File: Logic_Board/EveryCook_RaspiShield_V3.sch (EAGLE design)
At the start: 95 parts, among them IC1 TLP281-4, IC2 TLP281-4, J1 6P-2.54mm, J4 6P-2.54mm, J5 JUMPERSMD, Q2 IRLZ44N, U1 AD7794BRUZ, U2 PCA9685PW, U4 78M05, U7 CJ1117-3.3

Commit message: Schematic of logic board finished, only audio amp missing. Board ripped up for redraw
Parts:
- removed C4: 100uF/16V, Discrete:CAP-ELECTRO-C
- removed C8: 0.1uF, Discrete:C-0603
- removed D3: M7, Discrete:D-SMA
- removed IC1: TLP281-4, IC:TLP521-4
- removed J1: 6P-2.54mm, Connector:HEADER-6P-80/40MIL
- removed J14: (no value), Connector:HEADER-2P-5.0
- removed J4: 6P-2.54mm, Connector:HEADER-6P-65/35MIL
- removed J5: JUMPERSMD, Discrete:JUMPERSMD
- removed L2: 47uH, Discrete:L0630
- removed R1, R10, R11, R12, R13, R18, R19, R20, R21, R26, R27, R28, R29, R6, R7, R8, R9: 1k, Discrete:R-0603
- removed R14: 51k, Discrete:R-0603
- removed R15, R22, R23, R24, R25: 10k, Discrete:R-0603
- removed R16: 2k, Discrete:R-0603
- removed R5: 4.7k, Discrete:R-0603
- removed U$2: LM2596, IC:LM2596
- removed U13, U14, U15, U16, U17: (no value), Connector:RJ45-N
- removed U2: PCA9685PW, wia:PCA9685PW
- added BUT1, BUT2, BUT3, C_CLOSE, C_LOCK, FAN, I2C, P_LOCK, THSTAT_POT: (no value), pinhead:PINHD-1X2
- added C14: 22pF, Discrete:C-0603
- added C15: 0.1uF, Discrete:C-0603
- added DISPLAY, POWR_BRD: (no value), pinhead:PINHD-2X6
- added Q1: 8 MHz, crystal:CRYSTALHC49UP
- added Q3: BSP372, infineon:BSP613P
- added R3, R40, R45, R46: 10k, Discrete:R-0603
- added R39, R4, R44, R47, R48: 1k, Discrete:R-0603
- added T2: (no value), zetex:NPN_PNPSM8
- added VALVE+PROXSW: (no value), pinhead:PINHD-1X4
- added X1, X2, X3, X4, X5: MINI-USB_4P-85-32006-601-1, con-cypressindustries:MINI-USB_4P-85-32006-601-1
- C3: value 220uF/35V -> 22pF; device Discrete:CAP-ELECTRO-G -> Discrete:C-0603
- IC2: value TLP281-4 -> ATMEGA644A; device IC:TLP521-4 -> atmel:ATMEGA644A
- Q2: value IRLZ44N -> BSP372; device Discrete:MOSFET-N-D2PAK -> infineon:BSP613P; IMAX (none) -> 1.7A; MF (none) -> Infineon; VMAX (none) -> 100V
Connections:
- removed net +24V: C2.+, C3.+, J2.2, U$2.VIN, U4.IN
- removed net 3V3: C10.2, C17.2, C18.2, C6.+, C9.2, IC1.10, IC1.12, IC1.14, IC1.16, R26.2, R27.2, R28.2, R29.2, U1.DVDD, U16.2, U16.6, U16.8, U17.10, U17.9, U2.VDD, U7.OUT, U7.TAB
- removed net BUTTON: IC2.11, IC2.13, IC2.15, IC2.9, J4.2
- removed net CS: U$1.24-SPI-CE0-N, U1.~CS
- removed net D5V: C1.+, C4.+, C8.2, J5.2, L2.2, U$2.FB, U15.6, U7.IN
- removed net GPIO1: R41.2, U$1.11-GPIO0, U16.1
- removed net GPIO2: R42.2, U$1.13-GPIO2, U16.3
- removed net KEY1: IC2.16, R5.1
- removed net KEY1S: IC2.2, U$1.12-GPIO1
- removed net KEY2: IC2.14, R14.1
- removed net KEY2S: IC2.4, U$1.16-GPIO4
- removed net KEY3: IC2.12, R15.1
- removed net KEY3S: IC2.6, U$1.18-GPIO5
- removed net KEY4: IC2.10, R16.1
- removed net KEY4S: IC2.8, U$1.22-GPIO6
- removed net LED: IC1.2, J4.3
- removed net LED-1: R6.2, U17.1
- removed net LED-2: R7.2, U17.2
- removed net LED-3: R8.2, U17.3
- removed net LED-4: R9.2, U17.4
- removed net LED-5: R10.2, U17.5
- removed net LED-6: R11.2, U17.6
- removed net LED-7: R12.2, U17.7
- removed net LED-8: R13.1, U17.8
- removed net LED1: IC1.4, J4.4
- removed net LED1S: IC1.13, R23.2, U$1.8-TX
- removed net LED2: IC1.6, J4.5
- removed net LED2S: IC1.11, R24.2, U$1.10-RX
- removed net LED3: IC1.8, J4.6
- removed net LED3S: IC1.9, R25.2, U$1.26-SPI-CE1-N
- removed net LEDS: IC1.15, R22.2, U$1.7-GPIO7
- removed net MVCC: J14.1, J3.1
- removed net N$13: R1.2, U2.LED0
- removed net N$14: J1.2, U2.LED11
- removed net N$20: IC1.1, R18.1
- removed net N$21: IC1.3, R19.1
- removed net N$22: IC1.5, R20.1
- removed net N$23: IC1.7, R21.1
- removed net N$25: R6.1, U2.LED2
- removed net N$26: R7.1, U2.LED3
- removed net N$27: R8.1, U2.LED4
- removed net N$28: R9.1, U2.LED5
- removed net N$29: R10.1, U2.LED6
- removed net N$3: Q2.G, R1.1
- removed net N$30: R11.1, U2.LED7
- removed net N$31: R12.1, U2.LED8
- removed net N$32: R13.2, U2.LED9
- removed net N$33: J1.3, U2.LED12
- removed net N$34: J1.4, U2.LED13
- removed net N$35: J1.5, U2.LED14
- removed net N$36: J1.6, U2.LED15
- removed net N$4: J1.1, U2.LED10
- removed net N$67: IC2.1, R26.1
- removed net N$68: IC2.3, R27.1
- removed net N$69: IC2.5, R28.1
- removed net N$70: IC2.7, R29.1
- removed net N$91: U15.7
- removed net SCL: U$1.5-SCL0, U2.SCL
- removed net SDA: U$1.3-SDA0, U2.SDA
- removed net SERVO_SIG: U15.8, U2.LED1
- removed net VCC: J4.1, R14.2, R15.2, R16.2, R18.2, R19.2, R20.2, R21.2, R5.2
- new net +12V: C2.+, FAN.1, J3.1, U4.IN, VALVE+PROXSW.1
- new net +3V3: C10.2, C15.2, C17.2, C18.2, C6.+, C9.2, IC2.VCC, IC2.VCC@2, POWR_BRD.4, R3.2, R45.1, U1.DVDD, U7.OUT
- new net +5V: C1.+, J2.2, R46.2, T2A.E, U7.IN
- new net DAEMON_RST_LINE: IC2.(PCINT16/SCL)PC0, R44.1
- new net FAN_PWM: Q2.G, R4.1
- new net IH_OFF: IC2.(PCINT26/INT0)PD2, POWR_BRD.9
- new net IH_ON: POWR_BRD.5
- new net IH_PWR: IC2.(PCINT30/OC2B/ICP)PD6, POWR_BRD.1
- new net IH_RUN: IC2.(PCINT27/INT1)PD3, POWR_BRD.7
- new net IH_THERMISTOR: IC2.(PCINT1/ADC1)PA1, POWR_BRD.2, R40.2
- new net MOT_PWM: IC2.(PCINT29/OC1A)PD5, POWR_BRD.3
- new net N$10: IC2.(PCINT31/OC2A)PD7, R4.2
- new net N$11: DISPLAY.12, IC2.(PCINT18/TCK)PC2
- new net N$12: I2C.2, U$1.3-SDA0
- new net N$15: DISPLAY.11, IC2.(PCINT19/TMS)PC3
- new net N$16: DISPLAY.10, IC2.(PCINT20/TDO)PC4
- new net N$17: DISPLAY.9, IC2.(PCINT21/TDI)PC5
- new net N$18: DISPLAY.8, IC2.(PCINT22/TOSC1)PC6
- new net N$19: DISPLAY.7, IC2.(PCINT23/TOSC2)PC7
- new net N$37: DISPLAY.6, IC2.(PCINT8/XCK0/T0)PB0
- new net N$38: DISPLAY.5, IC2.(PCINT9/CLKO/T1)PB1
- new net N$39: DISPLAY.4, IC2.(PCINT10/INT2/AIN0)PB2
- new net N$41: DISPLAY.3, IC2.(PCINT11/OC0A/AIN1)PB3
- new net N$43: DISPLAY.1, IC2.(PCINT12/OC0B/!SS!)PB4
- new net N$49: DISPLAY.2, IC2.(PCINT0/ADC0)PA0
- new net N$50: I2C.1, U$1.5-SCL0
- new net N$51: FAN.2, Q2.D@1
- new net N$52: IC2.(PCINT24/RXD0)PD0, U$1.8-TX
- new net N$54: IC2.(PCINT25/TXD0)PD1, U$1.10-RX
- new net N$55: IC2.(PCINT14/MISO)PB6, U$1.16-GPIO4
- new net N$56: IC2.(PCINT13/MOSI)PB5, U$1.12-GPIO1
- new net N$59: C_CLOSE.1, IC2.(PCINT7/ADC7)PA7
- new net N$6: IC2.RESET, R3.1
- new net N$60: C_LOCK.1, IC2.(PCINT6/ADC6)PA6
- new net N$61: IC2.(PCINT5/ADC5)PA5, P_LOCK.1
- new net N$62: BUT2.1
- new net N$63: BUT3.1
- new net N$64: R39.2
- new net N$66: BUT1.1, R39.1, R44.2, R45.2
- new net N$7: C14.1, IC2.XTAL1, Q1.1
- new net N$71: R47.2, T2B.B
- new net N$72: R46.1, T2A.B, T2B.C1
- new net N$77: Q3.D@1, VALVE+PROXSW.2
- new net N$8: IC2.(PCINT15/SCK)PB7, U$1.18-GPIO5
- new net PROX_SWI: IC2.(PCINT2/ADC2)PA2, VALVE+PROXSW.3
- new net RPI_RST: IC2.(PCINT17/SDA)PC1, R47.1
- new net SAFETY_CHAIN: IC2.(PCINT4/ADC4)PA4
- new net VALVE_OPEN: Q3.G, R48.1
- net GND: now also BUT1.2, BUT2.2, BUT3.2, C14.2, C15.1, C3.2, C_CLOSE.2, C_LOCK.2, IC2.GND, IC2.GND@3, P_LOCK.2, Q2.S, Q3.S, R40.1, T2B.E, THSTAT_POT.2, U1.~CS, VALVE+PROXSW.4, X1.4, X2.4, X3.4, X4.4, X5.4; no longer C3.-, C4.-, C8.1, D3.+, R22.1, R23.1, R24.1, R25.1, U$2.GND, U$2.ON/OFF, U13.3, U13.4, U14.3, U14.4, U15.3, U15.4, U16.5, U2.A0, U2.A1, U2.A2, U2.A3, U2.A4, U2.A5, U2.EXTCLK, U2.VSS, U2.~OE, U4.GND
- net GPIO3: no longer U$1.15-GPIO3, U16.7
- net L5V: now also X1.1, X2.1, X3.1, X4.1, X5.1; no longer U13.5, U13.6, U14.5, U14.6, U15.5
- net LOADCELL1_SIG+: now also X2.2; no longer U13.7
- net LOADCELL1_SIG-: now also X2.3; no longer U13.8
- net LOADCELL2_SIG+: now also X1.2; no longer U13.1
- net LOADCELL2_SIG-: now also X1.3; no longer U13.2
- net LOADCELL3_SIG+: now also X4.2; no longer U14.7
- net LOADCELL3_SIG-: now also X4.3; no longer U14.8
- net LOADCELL4_SIG+: now also X3.2; no longer U14.1
- net LOADCELL4_SIG-: now also X3.3; no longer U14.2
- net N$2: now also C3.1, IC2.XTAL2, Q1.2; no longer J14.2, Q2.D
- net N$58: now also T2A.C1; no longer J5.1
- net N$65: now also IC2.(PCINT3/ADC3)PA3, R48.2; no longer D3.-, L2.1, U$2.OUTPUT
- net PGND: no longer Q2.S, U13.10, U13.9, U14.10, U14.9, U15.10, U15.9, U16.10, U16.9
- net PRESS_SIG+: now also X5.2; no longer U15.1
- net PRESS_SIG-: now also X5.3; no longer U15.2
- net TEMPER_SIG+: now also THSTAT_POT.1; no longer U16.4
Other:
- note removed: "7-Seg LED Conn."
- note removed: "Motor Conn."
- note removed: "PT 1000"
- note removed: "Reserve PWM Pads"
- note removed: "black"
- note removed: "blue"
- note removed: "bluew"
- note removed: "brown"
- note removed: "brownw"
- note removed: "button 2"
- note removed: "button 3"
- note removed: "button1"
- note removed: "green"
- note removed: "greenw"
- note removed: "on RJ45 cable"
- note removed: "on loadcells"
- note removed: "red"
- note removed: "redw"
- note removed: "servo brown"
- note removed: "servo orange"
- note removed: "servo red"
- note removed: "sig -"
- note removed: "sig 5V"
- note removed: "sig gnd"
- note removed: "sig+"
- note removed: "white"
- moved on the sheet: C1, C10, C12, C17, C18, C2, C6, C7, J2, J3, U4, U7

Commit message: Logic board all routed...
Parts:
- removed R41, R42, R43: 10k, Discrete:R-0603
- removed THSTAT_POT: (no value), pinhead:PINHD-1X2
- removed U$1: RASPBERRY-PI, RaspberryPi:RASPBERRY-PI
- added AIN_GND, AIN_SIG: (no value), wirepad:2,15/1,0
- added C16, C8: 10uF, Discrete:C-0603
- added C38: 100uF/25V, Discrete:CAP-ELECTRO-B
- added C4: 220pF, Discrete:C-0603
- added IC1: LM386MM-1, linear:LM386MM-1
- added R1, R5: 5k, Discrete:R-0603
- added R6, R7: 10k, Discrete:R-0603
- added RASPI_CONNECTOR_(TOP): (no value), pinhead:PINHD-2X13
- added SP1: AL23P, buzzer:AL23P
- added TEMP: (no value), pinhead:PINHD-1X2
- R3: value 10k -> 22k
- T2: value (none) -> ZDT6790
- renumbered X1 to LC2, X2 to LC1, X3 to LC4, X4 to LC3, X5 to PRESS
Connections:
- removed net GPIO3: R43.2
- removed net N$40: U$1.19-SPI-MOSI, U1.DIN
- new net MOSI: RASPI_CONNECTOR_(TOP).19, U1.DIN
- new net N$14: IC1.+IN, R1.2, R5.1
- new net N$22: C16.1, C38.+, IC1.OUT
- new net N$23: C38.-, SP1.1
- new net N$27: AIN_SIG.P, C4.2
- new net N$3: C4.1, R5.2
- net +3V3: now also IC2.AVCC, IC2.VCC@1, R6.1, R7.1
- net +5V: now also C16.2, IC1.VS
- net GND: now also AIN_GND.P, C8.1, IC1.-IN, IC1.GND, IC2.GND@1, IC2.GND@2, R1.1, RASPI_CONNECTOR_(TOP).6, SP1.2, TEMP.2; no longer R41.1, R42.1, R43.1, THSTAT_POT.2, U$1.6-GND
- net IH_ON: now also IC2.(PCINT28/OC1B)PD4
- net MISO: now also RASPI_CONNECTOR_(TOP).21; no longer U$1.21-SPI-MISO
- net N$12: now also RASPI_CONNECTOR_(TOP).3; no longer U$1.3-SDA0
- net N$50: now also RASPI_CONNECTOR_(TOP).5; no longer U$1.5-SCL0
- net N$52: now also RASPI_CONNECTOR_(TOP).8; no longer U$1.8-TX
- net N$54: now also RASPI_CONNECTOR_(TOP).10; no longer U$1.10-RX
- net N$55: now also RASPI_CONNECTOR_(TOP).16; no longer U$1.16-GPIO4
- net N$56: now also RASPI_CONNECTOR_(TOP).12; no longer U$1.12-GPIO1
- net N$58: now also RASPI_CONNECTOR_(TOP).2; no longer U$1.2-+5V
- net N$6: now also C8.2, RASPI_CONNECTOR_(TOP).11
- net N$62: now also R7.2, RASPI_CONNECTOR_(TOP).24
- net N$63: now also R6.2, RASPI_CONNECTOR_(TOP).26
- net N$64: now also RASPI_CONNECTOR_(TOP).22
- net N$8: now also RASPI_CONNECTOR_(TOP).18; no longer U$1.18-GPIO5
- net SAFETY_CHAIN: now also POWR_BRD.11
- net SCLK: now also RASPI_CONNECTOR_(TOP).23; no longer U$1.23-SPI-SCLK
- net TEMPER_SIG+: now also TEMP.1; no longer THSTAT_POT.1

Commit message: changed all 0606 to 0805 package for R and C.
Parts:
- C10, C11, C12, C14, C15, C16, C17, C18, C19, C20, C21, C22, C23, C24, C25, C26, C27, C28, C29, C3, C30, C31, C32, C33, C34, C35, C36, C37, C4, C5, C9: device Discrete:C-0603 -> rcl:C-EUC0805
- C13: device Discrete:C-0805 -> rcl:C-EUC0805
- C8: value 10uF -> 100nF; device Discrete:C-0603 -> rcl:C-EUC0805
- R1, R17, R3, R30, R31, R32, R33, R34, R35, R36, R37, R38, R39, R4, R40, R44, R45, R46, R47, R48, R5, R6, R7: device Discrete:R-0603 -> rcl:R-EU_R0805
- R2: value 22k -> 2.2k; device Discrete:R-0603 -> rcl:R-EU_R0805
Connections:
- net +3V3: now also U7.TAB
- net GND: now also U4.GND
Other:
- note removed: "KE43------ ON/OFF"
- note removed: "KEY1--------FUNSION"
- note removed: "KEY2------ -"
- note removed: "KEY3------ +"
- note removed: "SIG1--------MIN"
- note removed: "SIG2--------POWER"
- note removed: "SIG3--------MAX"
- note removed: "SIG4--------HOTPOT"
- note removed: "SIG5--------MID"
- note removed: "SIG6--------HEAT"
- moved on the sheet: C1, C2, C6, C7, J2, J3, LC1, LC2, LC3, LC4, PRESS, U4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

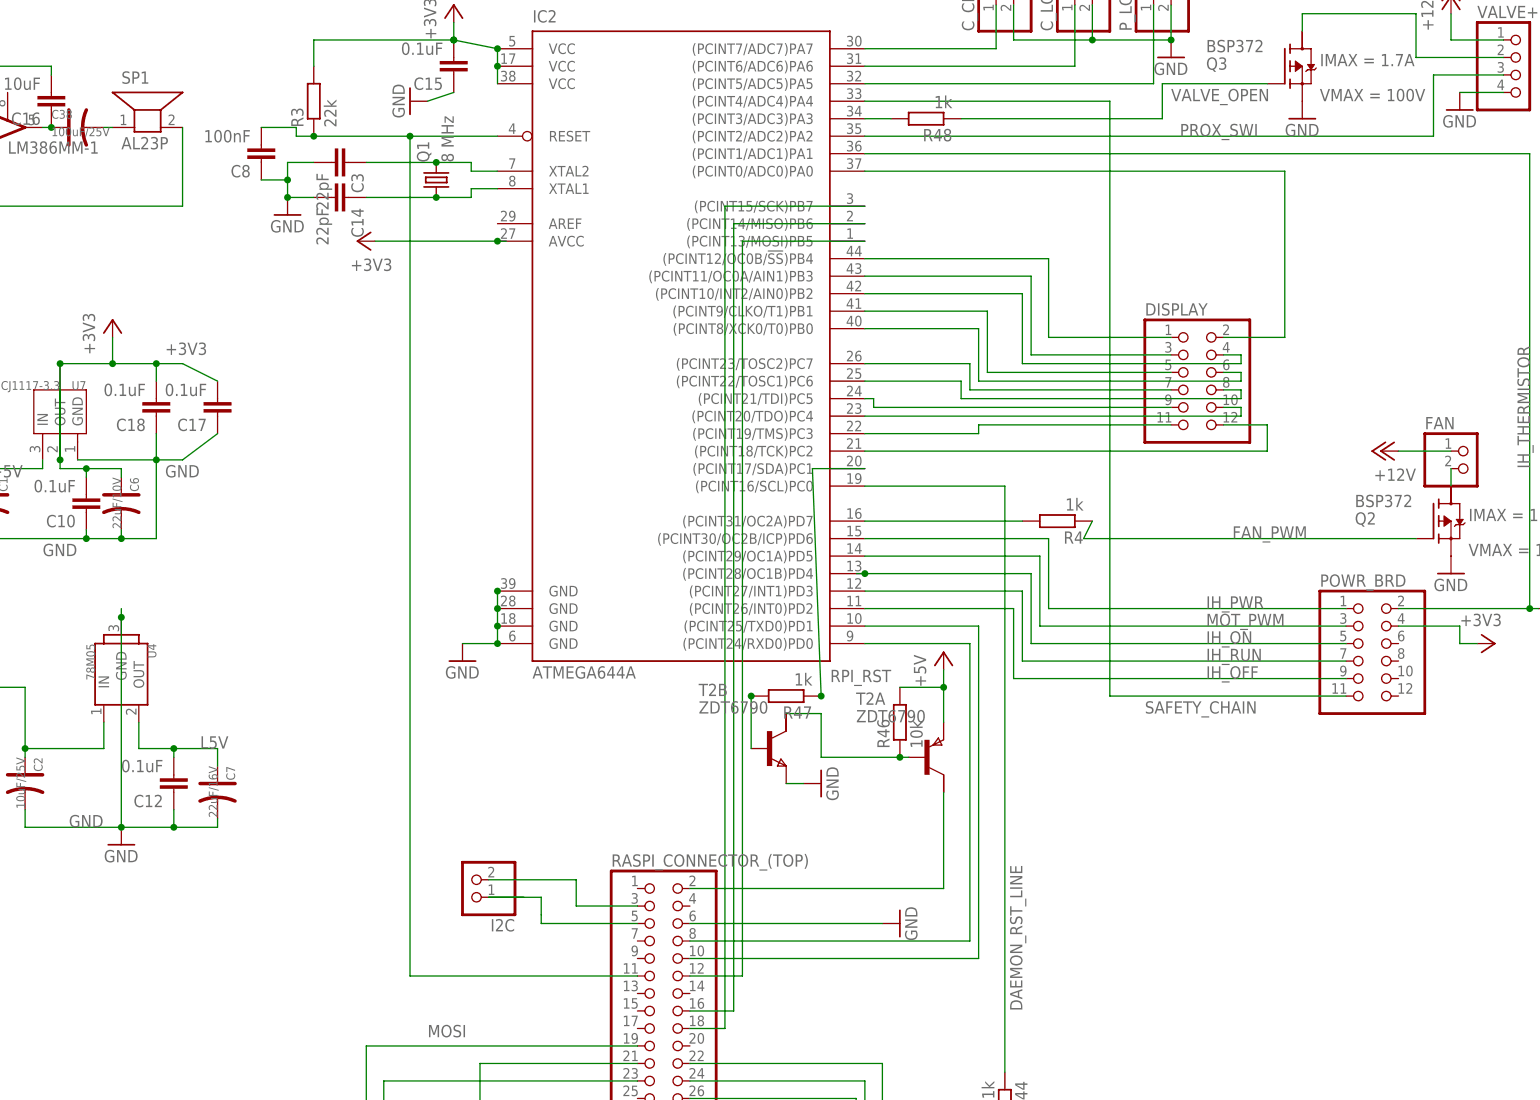
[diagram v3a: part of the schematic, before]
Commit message: Cleaned up the logic board. added safety chain board.
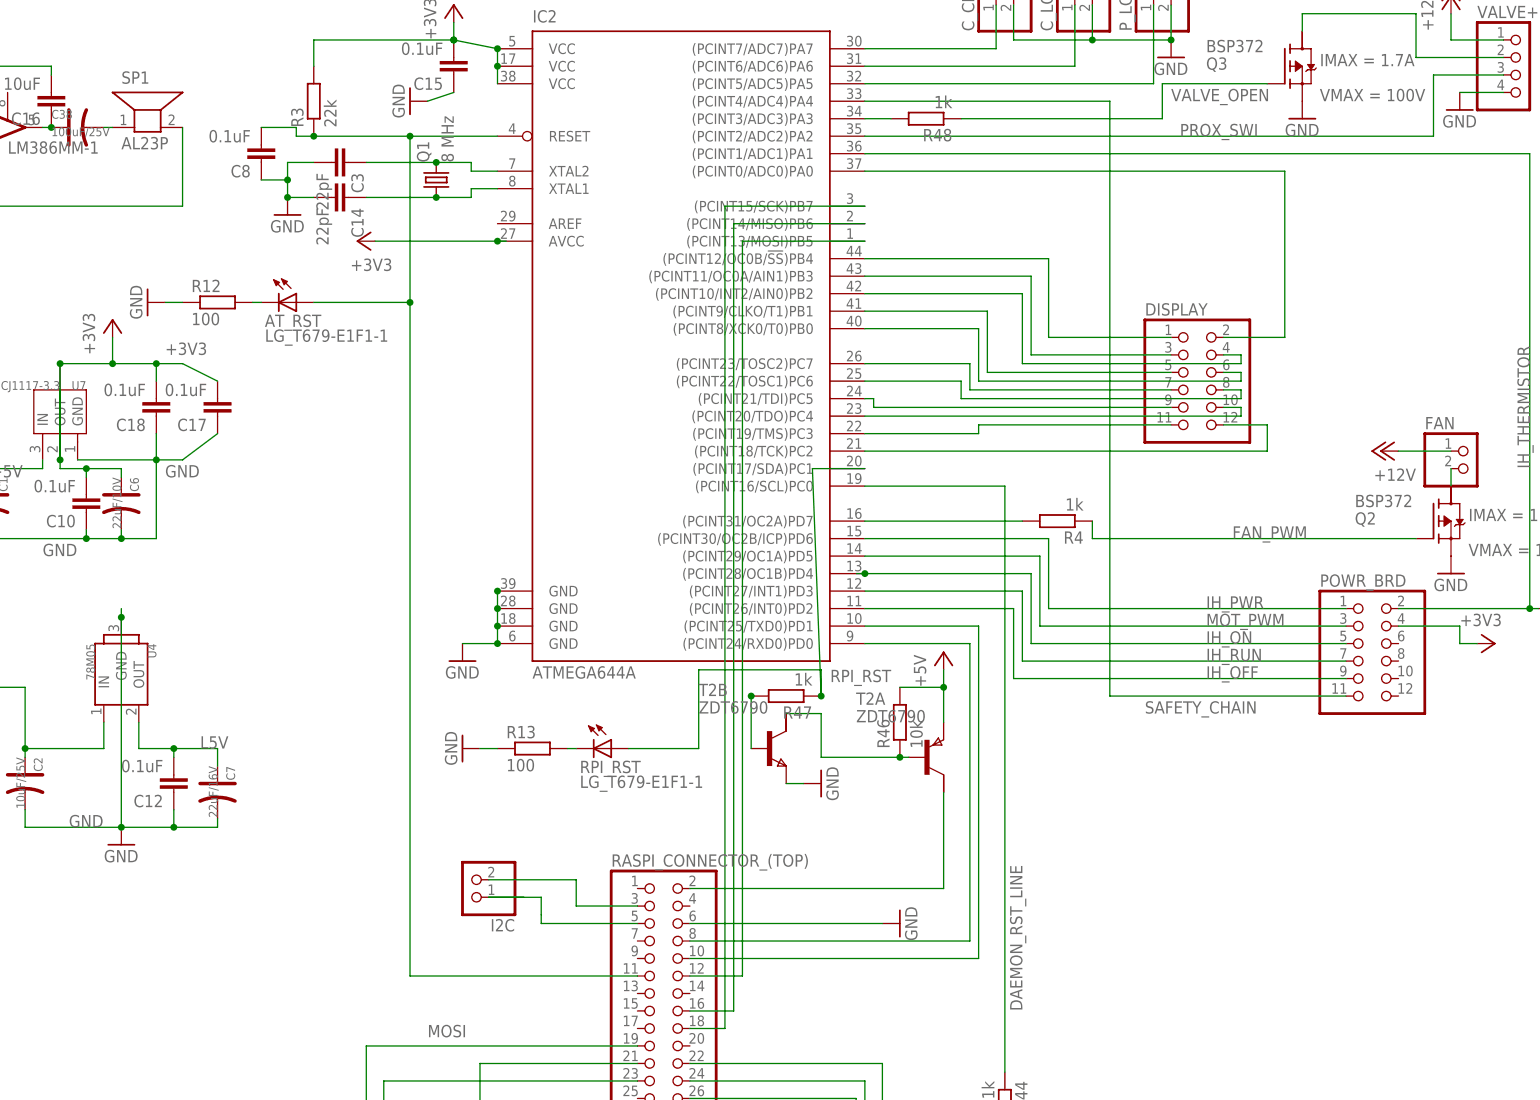
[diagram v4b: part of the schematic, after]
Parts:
- added AT_RST, RPI_RST: LG_T679-E1F1-1, led:LG_T679-E1F1-1
- added R12, R13: 100, rcl:R-EU_R0805
- C8: value 100nF -> 0.1uF
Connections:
- removed net N$6: C8.2, IC2.RESET, R3.1, RASPI_CONNECTOR_(TOP).11
- new net ATMEL_RST: AT_RST.A, C8.2, IC2.RESET, R3.1, RASPI_CONNECTOR_(TOP).11
- new net N$32: AT_RST.C, R12.2
- new net N$34: R13.2, RPI_RST.C
- net GND: now also R12.1, R13.1
- net RPI_RST: now also RPI_RST.A
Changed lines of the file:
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@@
 <setting verticaltext="up"/>
 </settings>
-<grid distance="0.05" unitdist="inch" unit="inch" style="lines" multiple="1" display="yes" altdistance="0.01" altunitdist="inch" altunit="inch"/>
+<grid distance="0.05" unitdist="inch" unit="inch" style="lines" multiple="1" display="no" altdistance="0.025" altunitdist="inch" altunit="inch"/>
 <layers>
 <layer number="1" name="Top" color="4" fill="1" visible="no" active="no"/>
@@
 <part name="R6" library="rcl" deviceset="R-EU_" device="R0805" value="10k"/>
 <part name="R7" library="rcl" deviceset="R-EU_" device="R0805" value="10k"/>
-<part name="C8" library="rcl" deviceset="C-EU" device="C0805" value="100nF"/>
+<part name="C8" library="rcl" deviceset="C-EU" device="C0805" value="0.1uF"/>
 <part name="GND25" library="supply1" deviceset="GND" device=""/>
+<part name="AT_RST" library="led" deviceset="*_T679-?-1" device="E1F1" technology="LG"/>
+<part name="R12" library="rcl" deviceset="R-EU_" device="R0805" value="100"/>
+<part name="GND30" library="supply1" deviceset="GND" device=""/>
+<part name="RPI_RST" library="led" deviceset="*_T679-?-1" device="E1F1" technology="LG"/>
+<part name="R13" library="rcl" deviceset="R-EU_" device="R0805" value="100"/>
+<part name="GND31" library="supply1" deviceset="GND" device=""/>
 </parts>
 <sheets>
@@
 <instance part="C8" gate="G$1" x="19.05" y="171.45" rot="R180"/>
 <instance part="GND25" gate="1" x="19.05" y="8.89" rot="R180"/>
+<instance part="AT_RST" gate="G$1" x="24.13" y="151.13" rot="R270"/>
+<instance part="R12" gate="G$1" x="12.7" y="151.13"/>
+<instance part="GND30" gate="1" x="2.54" y="151.13" rot="R270"/>
+<instance part="RPI_RST" gate="G$1" x="69.85" y="86.36" rot="R270"/>
+<instance part="R13" gate="G$1" x="58.42" y="86.36"/>
+<instance part="GND31" gate="1" x="48.26" y="86.36" rot="R270"/>
 </instances>
 <busses>
@@
 <pinref part="GND23" gate="1" pin="GND"/>
 </segment>
+<segment>
+<pinref part="R12" gate="G$1" pin="1"/>
+<pinref part="GND30" gate="1" pin="GND"/>
+<wire x1="7.62" y1="151.13" x2="5.08" y2="151.13" width="0.1524" layer="91"/>
+</segment>
+<segment>
+<pinref part="R13" gate="G$1" pin="1"/>
+<pinref part="GND31" gate="1" pin="GND"/>
+<wire x1="53.34" y1="86.36" x2="50.8" y2="86.36" width="0.1524" layer="91"/>
+</segment>
 </net>
 <net name="N$9" class="0">
@@
 </segment>
 </net>
-<net name="N$6" class="0">
-<segment>
-<pinref part="IC2" gate="G$1" pin="RESET"/>
-<wire x1="53.34" y1="175.26" x2="40.64" y2="175.26" width="0.1524" layer="91"/>
-<wire x1="40.64" y1="175.26" x2="40.64" y2="53.34" width="0.1524" layer="91"/>
-<pinref part="R3" gate="G$1" pin="1"/>
-<wire x1="40.64" y1="175.26" x2="26.67" y2="175.26" width="0.1524" layer="91"/>
-<junction x="40.64" y="175.26"/>
-<wire x1="40.64" y1="53.34" x2="73.66" y2="53.34" width="0.1524" layer="91"/>
-<pinref part="RASPI_CONNECTOR_(TOP)" gate="A" pin="11"/>
-<pinref part="C8" gate="G$1" pin="2"/>
-<wire x1="19.05" y1="176.53" x2="24.13" y2="176.53" width="0.1524" layer="91"/>
-<wire x1="24.13" y1="176.53" x2="24.13" y2="175.26" width="0.1524" layer="91"/>
-<wire x1="24.13" y1="175.26" x2="26.67" y2="175.26" width="0.1524" layer="91"/>
-<junction x="26.67" y="175.26"/>
-</segment>
-</net>
 <net name="N$2" class="0">
 <segment>
@@
 <pinref part="R4" gate="G$1" pin="1"/>
 <pinref part="Q2" gate="G$1" pin="G"/>
-<wire x1="186.69" y1="116.84" x2="138.43" y2="116.84" width="0.1524" layer="91"/>
-<wire x1="138.43" y1="116.84" x2="139.7" y2="119.38" width="0.1524" layer="91"/>
+<wire x1="186.69" y1="116.84" x2="139.7" y2="116.84" width="0.1524" layer="91"/>
+<wire x1="139.7" y1="116.84" x2="139.7" y2="119.38" width="0.1524" layer="91"/>
 <label x="160.02" y="116.84" size="1.778" layer="95"/>
 </segment>
@@
 <junction x="100.33" y="93.98"/>
 <label x="110.49" y="97.79" size="1.778" layer="95" rot="R180"/>
+<pinref part="RPI_RST" gate="G$1" pin="A"/>
+<wire x1="82.55" y1="86.36" x2="72.39" y2="86.36" width="0.1524" layer="91"/>
+<wire x1="82.55" y1="86.36" x2="82.55" y2="97.79" width="0.1524" layer="91"/>
+<wire x1="82.55" y1="97.79" x2="100.33" y2="97.79" width="0.1524" layer="91"/>
+<wire x1="100.33" y1="97.79" x2="100.33" y2="93.98" width="0.1524" layer="91"/>
 </segment>
 </net>
@@
 </segment>
 </net>
+<net name="ATMEL_RST" class="0">
+<segment>
+<pinref part="AT_RST" gate="G$1" pin="A"/>
+<wire x1="40.64" y1="151.13" x2="26.67" y2="151.13" width="0.1524" layer="91"/>
+<pinref part="IC2" gate="G$1" pin="RESET"/>
+<wire x1="53.34" y1="175.26" x2="40.64" y2="175.26" width="0.1524" layer="91"/>
+<wire x1="40.64" y1="175.26" x2="40.64" y2="151.13" width="0.1524" layer="91"/>
+<pinref part="R3" gate="G$1" pin="1"/>
+<wire x1="40.64" y1="151.13" x2="40.64" y2="53.34" width="0.1524" layer="91"/>
+<wire x1="40.64" y1="175.26" x2="26.67" y2="175.26" width="0.1524" layer="91"/>
+<junction x="40.64" y="175.26"/>
+<wire x1="40.64" y1="53.34" x2="73.66" y2="53.34" width="0.1524" layer="91"/>
+<pinref part="RASPI_CONNECTOR_(TOP)" gate="A" pin="11"/>
+<pinref part="C8" gate="G$1" pin="2"/>
+<wire x1="19.05" y1="176.53" x2="24.13" y2="176.53" width="0.1524" layer="91"/>
+<wire x1="24.13" y1="176.53" x2="24.13" y2="175.26" width="0.1524" layer="91"/>
+<wire x1="24.13" y1="175.26" x2="26.67" y2="175.26" width="0.1524" layer="91"/>
+<junction x="26.67" y="175.26"/>
+<junction x="40.64" y="151.13"/>
+</segment>
+</net>
+<net name="N$32" class="0">
+<segment>
+<pinref part="AT_RST" gate="G$1" pin="C"/>
+<pinref part="R12" gate="G$1" pin="2"/>
+<wire x1="19.05" y1="151.13" x2="17.78" y2="151.13" width="0.1524" layer="91"/>
+</segment>
+</net>
+<net name="N$34" class="0">
+<segment>
+<pinref part="RPI_RST" gate="G$1" pin="C"/>
+<pinref part="R13" gate="G$1" pin="2"/>
+<wire x1="64.77" y1="86.36" x2="63.5" y2="86.36" width="0.1524" layer="91"/>
+</segment>
+</net>
